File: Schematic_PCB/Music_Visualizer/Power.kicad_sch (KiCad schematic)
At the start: 16 parts, among them J2 PJ-079BH, Q1 DMP2123LQ-7, SW2 SW_SPST, U8 LT1054, U9 MC78L05_TO92

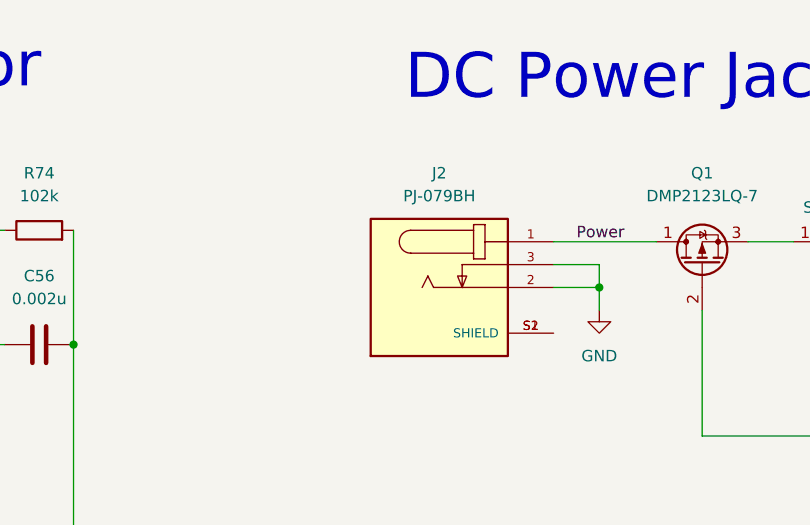
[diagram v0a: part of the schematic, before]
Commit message: RHi- Value controll replaced
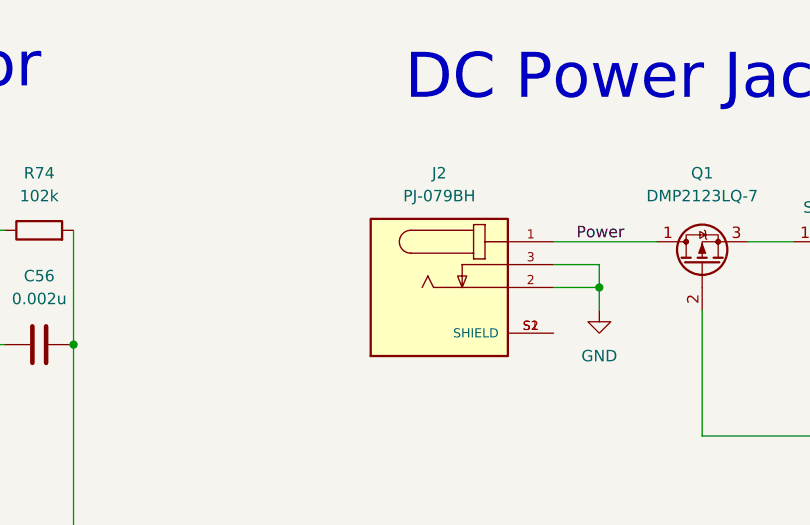
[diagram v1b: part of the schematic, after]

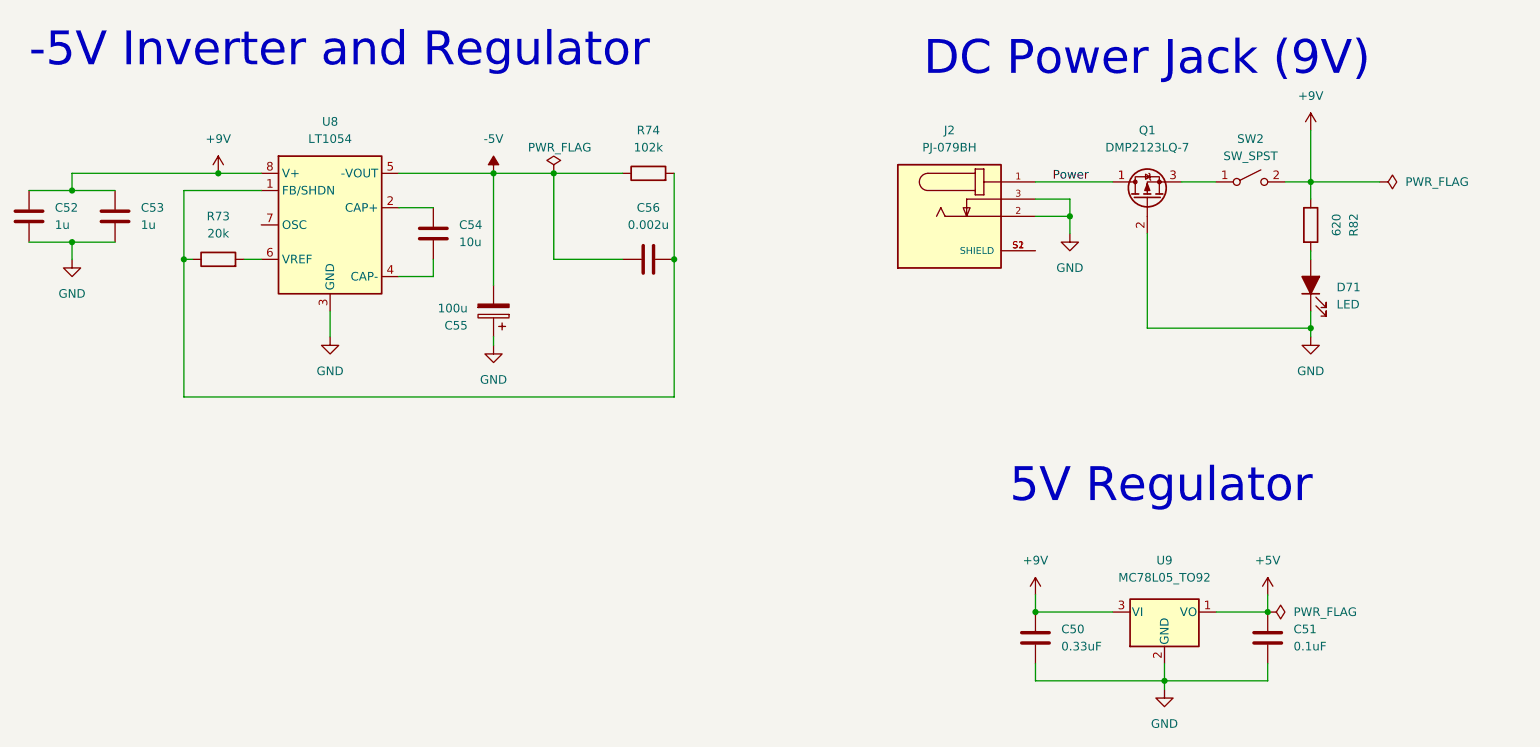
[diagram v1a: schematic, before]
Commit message: Replace +-5v with 9v
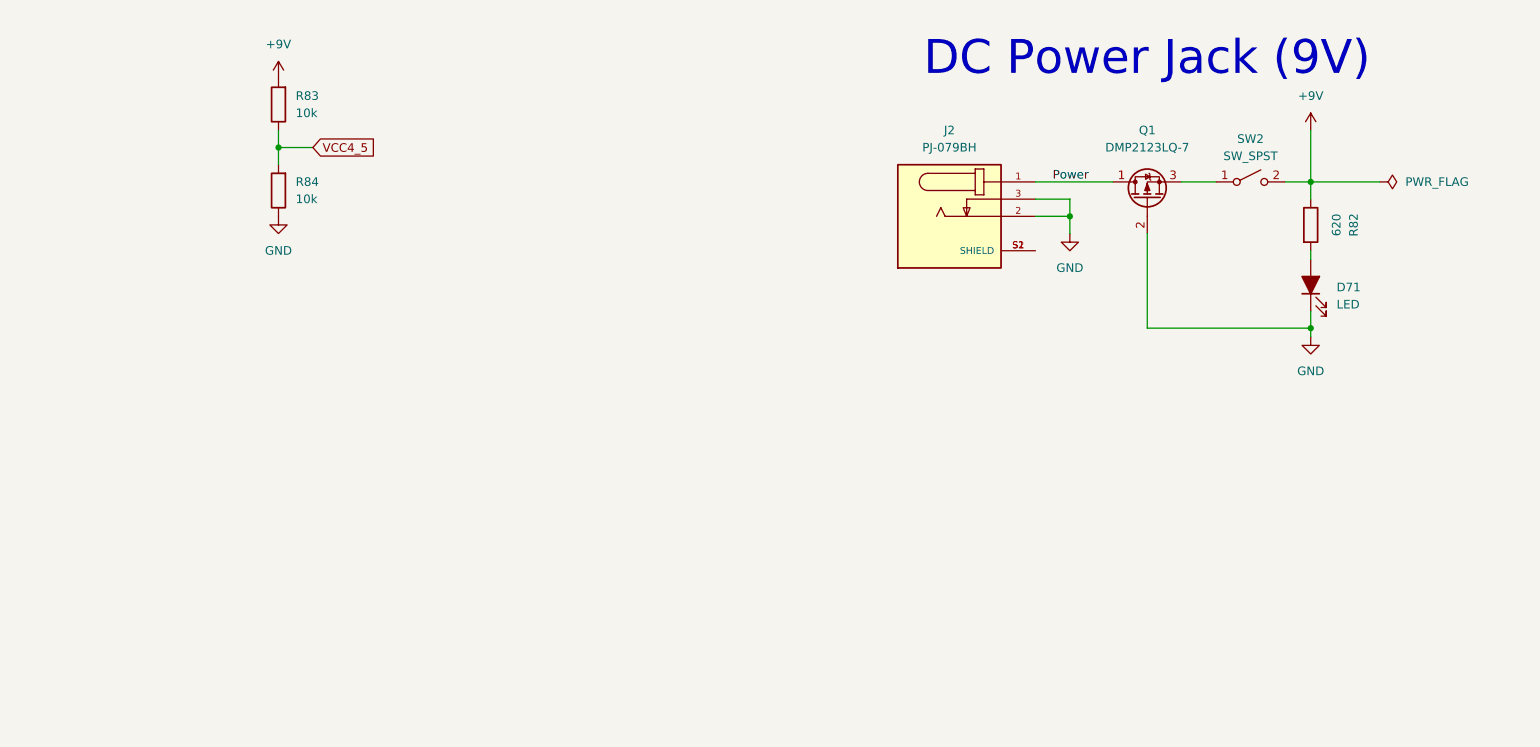
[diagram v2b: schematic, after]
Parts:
- removed C50: 0.33uF, Capacitor_SMD:C_0603_1608Metric_Pad1.08x0.95mm_HandSolder, symbol Device:C
- removed C51: 0.1uF, Capacitor_SMD:C_0805_2012Metric, symbol Device:C
- removed C52, C53: 1u, Capacitor_SMD:C_0603_1608Metric_Pad1.08x0.95mm_HandSolder, symbol Device:C
- removed C54: 10u, Capacitor_SMD:C_0805_2012Metric, symbol Device:C
- removed C55: 100u, Capacitor_THT:C_Radial_D5.0mm_H5.0mm_P2.00mm, symbol Device:C_Polarized
- removed C56: 0.002u, Capacitor_SMD:C_0603_1608Metric_Pad1.08x0.95mm_HandSolder, symbol Device:C
- removed R73: 20k, Resistor_SMD:R_0603_1608Metric_Pad0.98x0.95mm_HandSolder, symbol Device:R
- removed R74: 102k, Resistor_SMD:R_0603_1608Metric_Pad0.98x0.95mm_HandSolder, symbol Device:R
- removed U8: LT1054, LT1054_PDIP_Lin_Reg:DIP794W45P254L959H508Q8, symbol Regulator_SwitchedCapacitor:LT1054
- removed U9: MC78L05_TO92, Package_TO_SOT_THT:TO-92_Inline, symbol Regulator_Linear:MC78L05_TO92
- added R83, R84: 10k, Resistor_SMD:R_0603_1608Metric_Pad0.98x0.95mm_HandSolder, symbol Device:R
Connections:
- net +9V: now also R83.2
- net GND: now also R84.1
- new net VCC4_5: R83.1, R84.2
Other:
- note removed: "-5V Inverter and Regulator"
- note removed: "5V Regulator"

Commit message: Change op amp exit cap
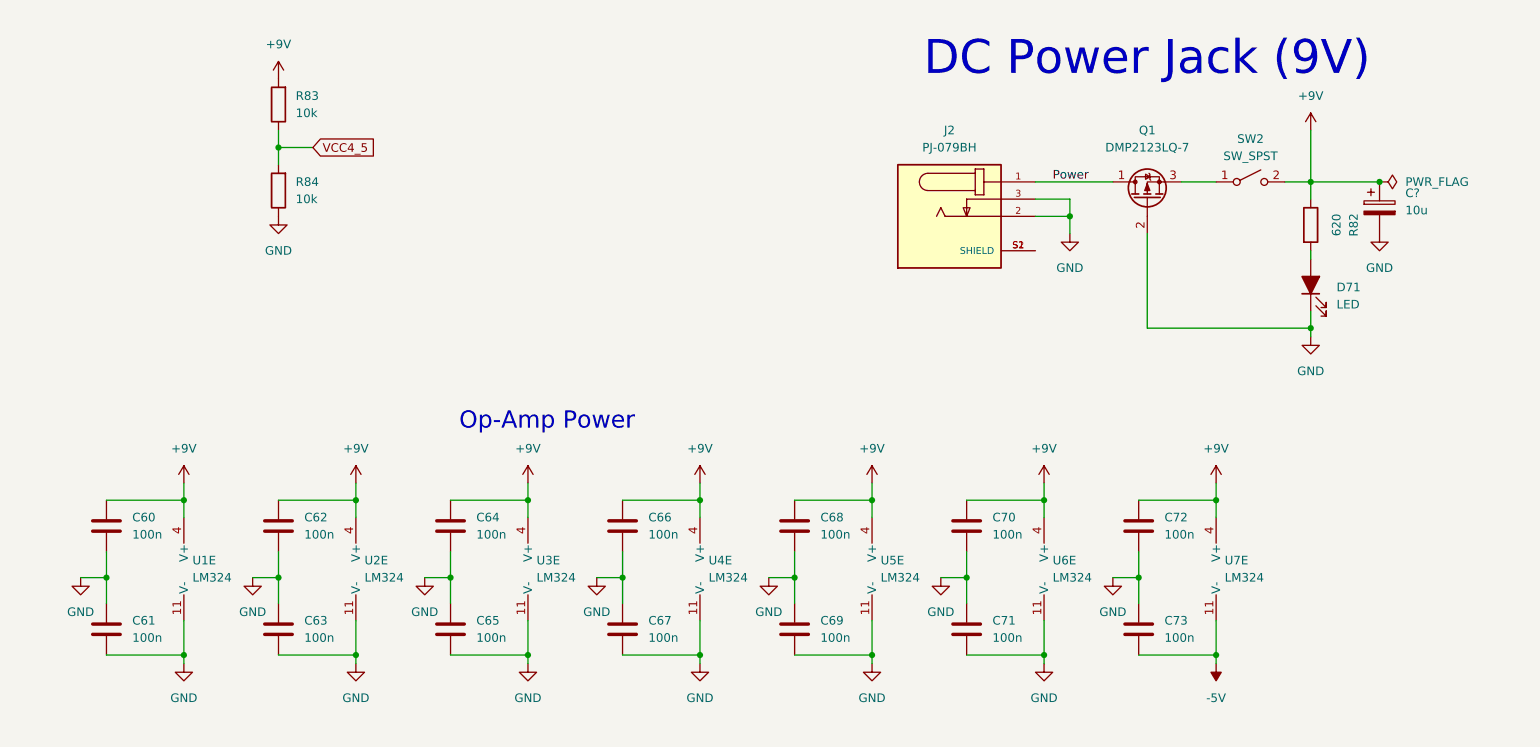
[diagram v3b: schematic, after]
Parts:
- added C60, C61, C62, C63, C64, C65, C66, C67, C68, C69, C70, C71, C72, C73: 100n, Capacitor_SMD:C_0805_2012Metric_Pad1.18x1.45mm_HandSolder, symbol Device:C
- added C?: 10u, Capacitor_THT:CP_Radial_D5.0mm_P2.00mm, symbol Device:C_Polarized
- added U1, U2, U3, U4, U5, U6, U7: LM324, Package_SO:SOIC-14_3.9x8.7mm_P1.27mm, symbol Amplifier_Operational:LM324
- D71: footprint LED_THT:LED_D5.0mm -> LED_SMD:LED_1210_3225Metric_Pad1.42x2.65mm_HandSolder
- R82, R83, R84: footprint Resistor_SMD:R_0603_1608Metric_Pad0.98x0.95mm_HandSolder -> Resistor_SMD:R_0805_2012Metric_Pad1.20x1.40mm_HandSolder
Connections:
- net +9V: now also C60.2, C62.2, C64.2, C66.2, C68.2, C70.2, C72.2, C?.1, U1.4 (V+), U2.4 (V+), U3.4 (V+), U4.4 (V+), U5.4 (V+), U6.4 (V+), U7.4 (V+)
- net GND: now also C60.1, C61.1, C61.2, C62.1, C63.1, C63.2, C64.1, C65.1, C65.2, C66.1, C67.1, C67.2, C68.1, C69.1, C69.2, C70.1, C71.1, C71.2, C72.1, C73.2, C?.2, U1.11 (V-), U2.11 (V-), U3.11 (V-), U4.11 (V-), U5.11 (V-), U6.11 (V-)
- new net -5V: C73.1, U7.11 (V-)
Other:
- note added: "Op-Amp Power"

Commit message: Add testpoints
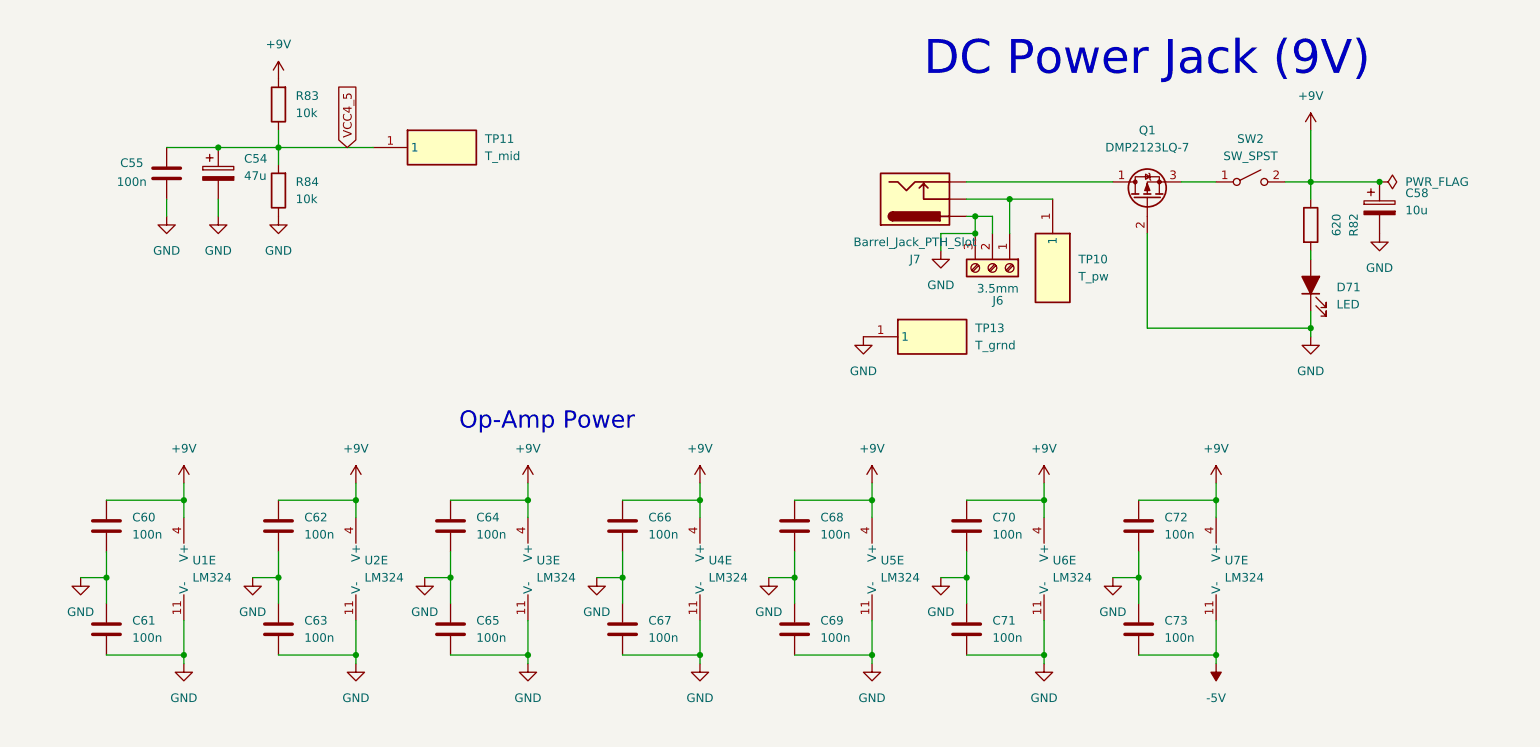
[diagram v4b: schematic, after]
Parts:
- removed J2: PJ-079BH, CUI_PJ-079BH, symbol DC_Power_Jack_PJ-079BH:PJ-079BH
- added C54: 47u, Capacitor_THT:CP_Radial_D5.0mm_P2.00mm, symbol Device:C_Polarized
- added C55: 100n, Capacitor_SMD:C_0805_2012Metric_Pad1.18x1.45mm_HandSolder, symbol Device:C
- added J6: 3.5mm, PCM_SparkFun-Connector:ScrewTerminal_1x03_P3.5mm_Horizontal_Black, symbol PCM_SparkFun-Connector:ScrewTerminal_1x03_P3.5mm_Horizontal_Black
- added J7: Barrel_Jack_PTH_Slot, PCM_SparkFun-Connector:Barrel_Jack_PTH_Slot, symbol PCM_SparkFun-Connector:Barrel_Jack_PTH_Slot
- added TP10: T_pw, Custom_Footprints:TEST1Y, symbol TEST-1_Y_:TEST-1_Y_
- added TP11: T_mid, Custom_Footprints:TEST1Y, symbol TEST-1_Y_:TEST-1_Y_
- added TP13: T_grnd, Custom_Footprints:TEST1Y, symbol TEST-1_Y_:TEST-1_Y_
- gave numbers to parts that had none: 1
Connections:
- net GND: now also C54.2, C55.1, J6.2 (Pin_2), J6.3 (Pin_3), J7.PWR, TP13.1
- net VCC4_5: now also C54.1, C55.2, TP11.1
- net Power: no longer names the net of Q1.1 (D)
- net Power: now also J7.GND
- new net: J6.1 (Pin_1), J7.GNDBREAK, TP10.1

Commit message: In-Out switch
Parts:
- SW2: footprint PW_On_Off_Switch:E-SWITCH_RR511D1121 -> Button_Switch_THT:SW_Slide-03_Wuerth-WS-SLTV_10x2.5x6.4_P2.54mm
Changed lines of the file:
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@@
 			)
 		)
-		(property "Footprint" "PW_On_Off_Switch:E-SWITCH_RR511D1121"
+		(property "Footprint" "Button_Switch_THT:SW_Slide-03_Wuerth-WS-SLTV_10x2.5x6.4_P2.54mm"
 			(at 201.93 52.07 0)
 			(effects

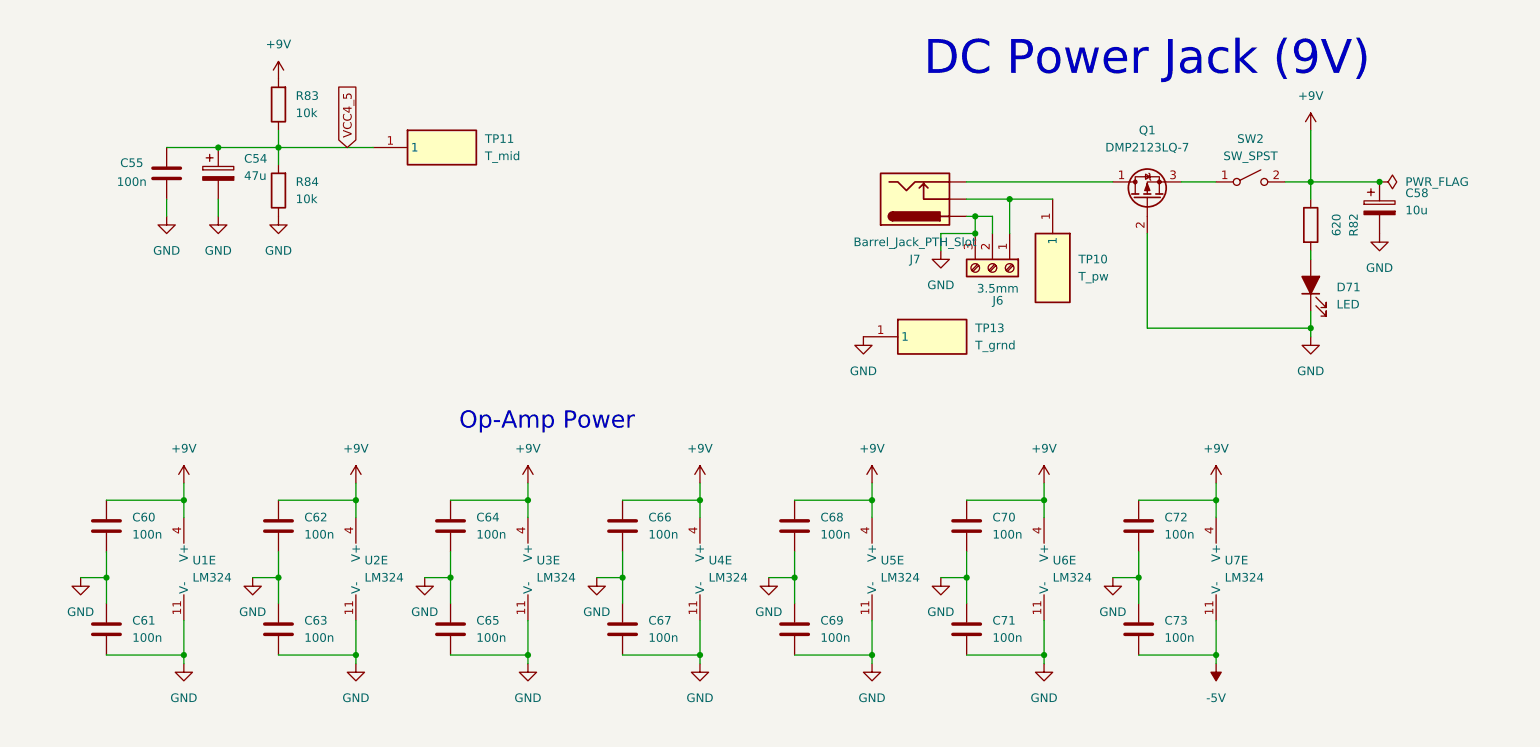
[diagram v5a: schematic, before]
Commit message: Correct op amps
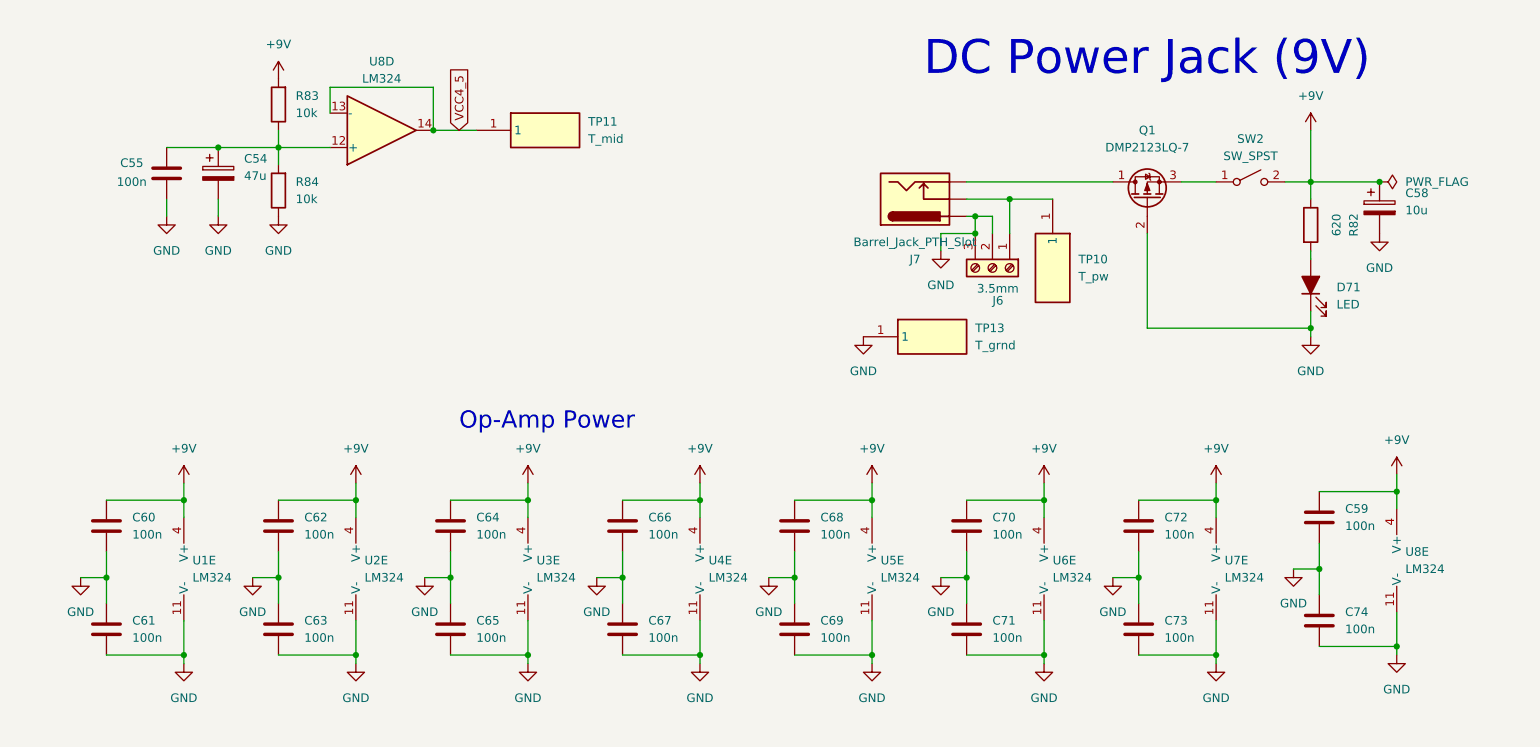
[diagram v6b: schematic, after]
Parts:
- added C59, C74: 100n, Capacitor_SMD:C_0805_2012Metric_Pad1.18x1.45mm_HandSolder, symbol Device:C
- added U8: LM324, Package_SO:SOIC-14_3.9x8.7mm_P1.27mm, symbol Amplifier_Operational:LM324
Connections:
- net -5V is gone; now on net GND: C73.1, U7.11 (V-)
- net +9V: now also C59.2, U8.4 (V+)
- net GND: now also C59.1, C74.1, C74.2, U8.11 (V-)
- net VCC4_5: now also U8.13 (-), U8.14; no longer C54.1, C55.2, R83.1, R84.2
- new net: C54.1, C55.2, R83.1, R84.2, U8.12 (+)
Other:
- moved on the sheet: TP11
